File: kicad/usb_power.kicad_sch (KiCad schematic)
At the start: 12 parts, among them J1 12402012E212A, U7 TLV73325PDBV, U8 TLV73333PDBV

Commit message: add fourth level converter for simultaneous programming + TX/RX
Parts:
- U7, U8: footprint riotee:TI_DBV0005A -> Package_TO_SOT_SMD:SOT-23-5
- renumbered R27 to R25, R28 to R26, R29 to R27
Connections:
- net +3V3: no longer C23.1, U7.1 (IN)
- net VBUS: now also C23.1, C24.1, D2.1 (K), U7.1 (IN), U8.1 (IN), U8.3 (EN); no longer D2.2 (A), J1.A4/B9 (VBUS), J1.B4/A9 (VBUS)
- new net: D2.2 (A), J1.A4/B9 (VBUS), J1.B4/A9 (VBUS)
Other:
- moved on the sheet: D2

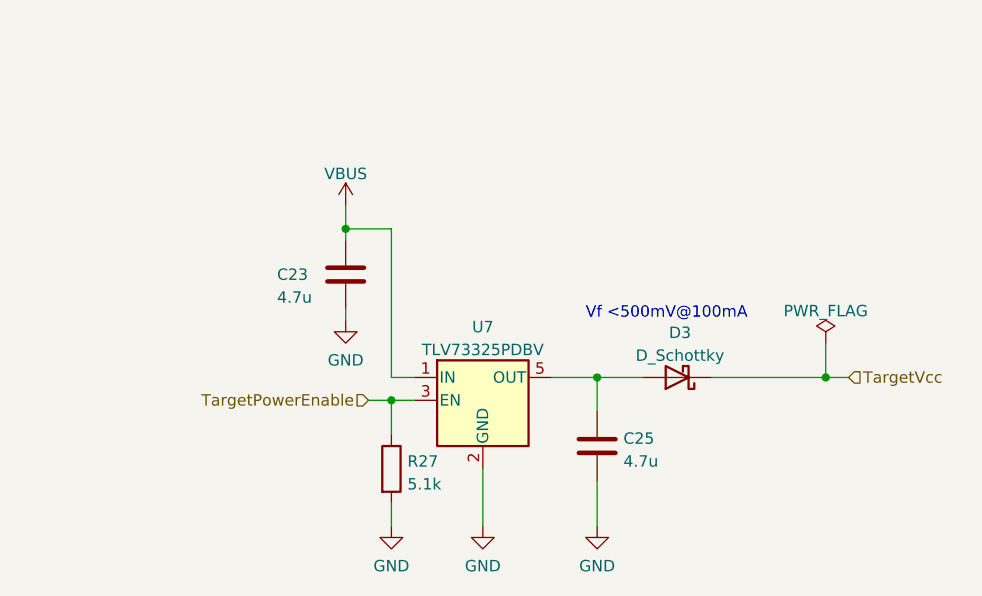
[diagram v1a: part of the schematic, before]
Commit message: replace target supply diode with analog switch
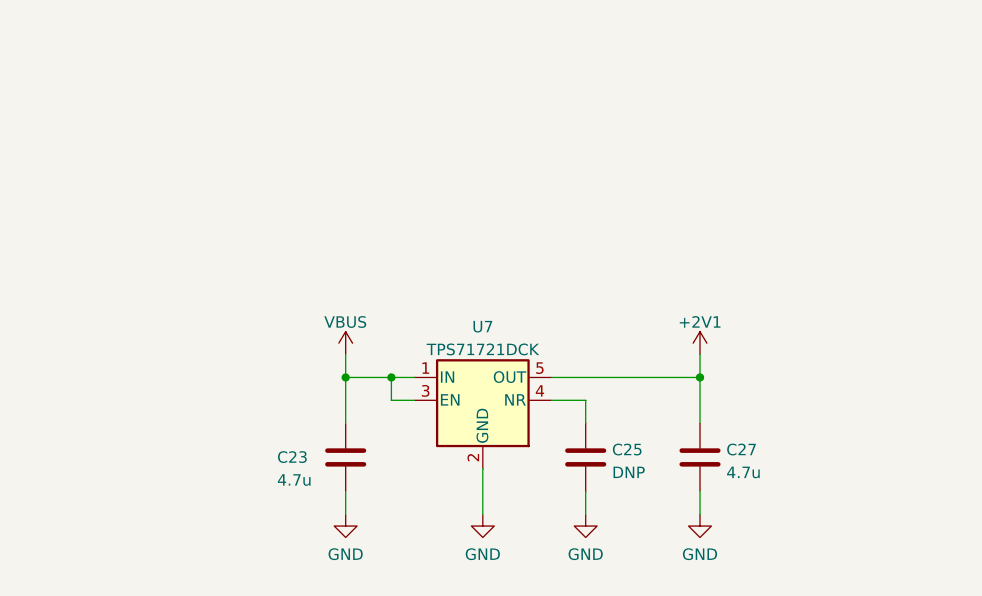
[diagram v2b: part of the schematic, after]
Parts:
- removed D3: D_Schottky, Diode_SMD:D_SOD-523, symbol Device:D_Schottky
- removed R27: 5.1k, Resistor_SMD:R_0402_1005Metric, symbol Device:R
- removed U7: TLV73325PDBV, Package_TO_SOT_SMD:SOT-23-5, symbol Regulator_Linear:TLV73325PDBV
- added C25: DNP, Capacitor_SMD:C_0402_1005Metric, symbol Device:C
- added U7: TPS71721DCK, riotee:TI_DCK0005A, symbol riotee:TPS71721DCK
- U8: footprint Package_TO_SOT_SMD:SOT-23-5 -> riotee:TI_DBV0005A
- renumbered C25 to C27
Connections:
- net GND: now also C25.2, U7.2 (GND)
- net VBUS: now also U7.1 (IN), U7.3 (EN)
- net +2V1: now reaches C27.1
- net +2V1: now also U7.5 (OUT)
- new net: C25.1, U7.4 (NR)
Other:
- note removed: "Vf <500mV@100mA"
- moved on the sheet: C23, C27

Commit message: add MPNs in schematics
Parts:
- C23, C24, C26, C27: MPN (none) -> CL05A475MP5NRNC
- D2: MPN (none) -> RB521S30T1G
- J1: MPN (none) -> 12402012E212A
- R25, R26: MPN (none) -> CR0402-FX-5101GLF
- U7: MPN (none) -> TPS71721DCK
- U8: MPN (none) -> TLV73333PDBV
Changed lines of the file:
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@@
+      (effects (font (size 1.27 1.27)) hide)
+    )
+    (property "MPN" "CL05A475MP5NRNC" (id 4) (at 190.5 58.42 0)
       (effects (font (size 1.27 1.27)) hide)
     )
@@
       (effects (font (size 1.27 1.27)) hide)
     )
+    (property "MPN" "TLV73333PDBV" (id 4) (at 205.74 54.61 0)
+      (effects (font (size 1.27 1.27)) hide)
+    )
     (pin "1")
     (pin "2")
@@
     )
     (property "Datasheet" "https://www.amphenol-cs.com/usb2-0-12402012e212a.html" (id 3) (at 90.17 127 0)
+      (effects (font (size 1.27 1.27)) hide)
+    )
+    (property "MPN" "12402012E212A" (id 4) (at 85.09 95.25 0)
       (effects (font (size 1.27 1.27)) hide)
     )
@@
       (effects (font (size 1.27 1.27)) hide)
     )
+    (property "MPN" "CL05A475MP5NRNC" (id 4) (at 218.44 58.42 0)
+      (effects (font (size 1.27 1.27)) hide)
+    )
     (pin "1")
     (pin "2")
@@
       (effects (font (size 1.27 1.27)) hide)
     )
+    (property "MPN" "CL05A475MP5NRNC" (id 4) (at 186.69 125.73 0)
+      (effects (font (size 1.27 1.27)) hide)
+    )
     (pin "1")
     (pin "2")
@@
     )
     (property "Datasheet" "~" (id 3) (at 111.76 116.84 0)
+      (effects (font (size 1.27 1.27)) hide)
+    )
+    (property "MPN" "CR0402-FX-5101GLF" (id 4) (at 111.76 116.84 0)
       (effects (font (size 1.27 1.27)) hide)
     )
@@
       (effects (font (size 1.27 1.27)) hide)
     )
+    (property "MPN" "TPS71721DCK" (id 4) (at 201.93 119.38 0)
+      (effects (font (size 1.27 1.27)) hide)
+    )
     (pin "1")
     (pin "2")
@@
       (effects (font (size 1.27 1.27)) hide)
     )
+    (property "MPN" "CL05A475MP5NRNC" (id 4) (at 226.06 125.73 0)
+      (effects (font (size 1.27 1.27)) hide)
+    )
     (pin "1")
     (pin "2")
@@
     )
     (property "Datasheet" "~" (id 3) (at 102.87 116.84 0)
+      (effects (font (size 1.27 1.27)) hide)
+    )
+    (property "MPN" "CR0402-FX-5101GLF" (id 4) (at 102.87 116.84 0)
       (effects (font (size 1.27 1.27)) hide)
     )
@@
       (effects (font (size 1.27 1.27)) hide)
     )
+    (property "MPN" "RB521S30T1G" (id 4) (at 110.49 80.01 0)
+      (effects (font (size 1.27 1.27)) hide)
+    )

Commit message: update footprints and add component description to BOM
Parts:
- C25: now left out of the parts list
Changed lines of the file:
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@@
+      (effects (font (size 1.27 1.27)) hide)
+    )
+    (property "Description" "Cap, 0402, X5R/X7R, 10V" (id 5) (at 190.5 58.42 0)
       (effects (font (size 1.27 1.27)) hide)
     )
@@
   )
   (symbol (lib_id "Device:C") (at 213.36 125.73 0) (unit 1)
-    (in_bom yes) (on_board yes) (fields_autoplaced)
+    (in_bom no) (on_board yes) (fields_autoplaced)
     (property "Reference" "C25" (id 0) (at 216.281 124.8953 0)
       (effects (font (size 1.27 1.27)) (justify left))
@@
     )
     (property "MPN" "TLV73333PDBV" (id 4) (at 205.74 54.61 0)
+      (effects (font (size 1.27 1.27)) hide)
+    )
+    (property "Description" "3.3V 300mA LDO" (id 5) (at 205.74 54.61 0)
       (effects (font (size 1.27 1.27)) hide)
     )
@@
       (effects (font (size 1.27 1.27)) hide)
     )
+    (property "Description" "Cap, 0402, X5R/X7R, 10V" (id 5) (at 218.44 58.42 0)
+      (effects (font (size 1.27 1.27)) hide)
+    )
     (pin "1")
     (pin "2")
@@
       (effects (font (size 1.27 1.27)) hide)
     )
+    (property "Description" "Cap, 0402, X5R/X7R, 10V" (id 5) (at 186.69 125.73 0)
+      (effects (font (size 1.27 1.27)) hide)
+    )
     (pin "1")
     (pin "2")
@@
     )
     (property "MPN" "CR0402-FX-5101GLF" (id 4) (at 111.76 116.84 0)
+      (effects (font (size 1.27 1.27)) hide)
+    )
+    (property "Description" "Res, 0402, 1%" (id 5) (at 111.76 116.84 0)
       (effects (font (size 1.27 1.27)) hide)
     )
@@
       (effects (font (size 1.27 1.27)) hide)
     )
+    (property "Description" "2.1V 150-mA LDO" (id 5) (at 201.93 119.38 0)
+      (effects (font (size 1.27 1.27)) hide)
+    )
     (pin "1")
     (pin "2")
@@
       (effects (font (size 1.27 1.27)) hide)
     )
+    (property "Description" "Cap, 0402, X5R/X7R, 10V" (id 5) (at 226.06 125.73 0)
+      (effects (font (size 1.27 1.27)) hide)
+    )
     (pin "1")
     (pin "2")
@@
     )
     (property "MPN" "CR0402-FX-5101GLF" (id 4) (at 102.87 116.84 0)
+      (effects (font (size 1.27 1.27)) hide)
+    )
+    (property "Description" "Res, 0402, 1%" (id 5) (at 102.87 116.84 0)
       (effects (font (size 1.27 1.27)) hide)
     )
@@
       (effects (font (size 1.27 1.27)) hide)
     )
+    (property "Description" "Schottky, IF >=100mA, Vf<0.5V" (id 5) (at 110.49 80.01 0)
+      (effects (font (size 1.27 1.27)) hide)
+    )

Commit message: add conformity marks and refine BOM settings
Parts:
- C25: now in the parts list
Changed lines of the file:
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@@
   )
   (symbol (lib_id "Device:C") (at 213.36 125.73 0) (unit 1)
-    (in_bom no) (on_board yes) (fields_autoplaced)
+    (in_bom yes) (on_board yes) (fields_autoplaced)
     (property "Reference" "C25" (id 0) (at 216.281 124.8953 0)
       (effects (font (size 1.27 1.27)) (justify left))
@@
       (effects (font (size 1.27 1.27)) hide)
     )
+    (property "Description" "CONN RCP USB2.0 TYP C 24P SMD RA" (id 5) (at 85.09 95.25 0)
+      (effects (font (size 1.27 1.27)) hide)
+    )

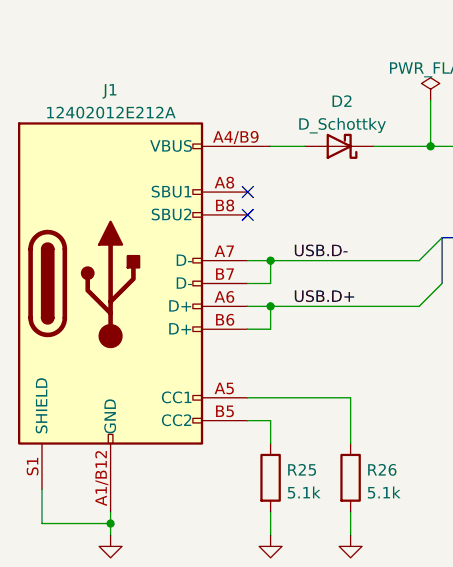
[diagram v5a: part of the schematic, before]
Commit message: migrate project to kicad 7
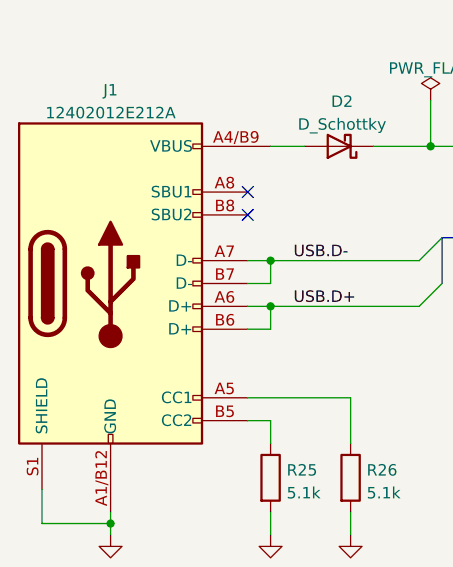
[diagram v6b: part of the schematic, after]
